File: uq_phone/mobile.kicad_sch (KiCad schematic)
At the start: 41 parts, among them J3 20279-001E-03, J4 20279-001E-03, J5 0786463001, Q1 MMBT3904, Q2 MMBT3904, U4 RC7620_1104625

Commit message: Update LCD, Add Programer, Shrink Footprints
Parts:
- R12, R17: value 4k7 -> 4.7k; footprint Resistor_SMD:R_0603_1608Metric -> Resistor_SMD:R_0402_1005Metric
- R13, R18: footprint Resistor_SMD:R_0603_1608Metric -> Resistor_SMD:R_0402_1005Metric
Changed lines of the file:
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@@
 		(pin "93"
 		)
-		(pin "244"
-		)
 		(pin "185"
 		)
@@
 		(pin "24"
 		)
-		(pin "243"
-		)
 		(pin "211"
 		)
@@
 		(pin "93"
 		)
-		(pin "244"
-		)
 		(pin "185"
 		)
@@
 		(pin "24"
 		)
-		(pin "243"
-		)
 		(pin "211"
 		)
@@
 			)
 		)
-		(property "Footprint" "Resistor_SMD:R_0603_1608Metric"
+		(property "Footprint" "Resistor_SMD:R_0402_1005Metric"
 			(at 67.31 257.81 0)
 			(effects
@@
 			)
 		)
-		(property "Description" ""
+		(property "Description" "RES SMD 47K OHM 1% 1/10W 0402"
 			(at 67.31 257.81 0)
 			(effects
@@
 	)
 	(symbol
-		(lib_name "RC7620_1104625_1")
 		(lib_id "RC7620_1104625:RC7620_1104625")
 		(at 200.66 97.79 0)
@@
 			)
 		)
-		(property "Value" "4k7"
+		(property "Value" "4.7k"
 			(at 115.57 246.38 90)
 			(effects
@@
 			)
 		)
-		(property "Footprint" "Resistor_SMD:R_0603_1608Metric"
+		(property "Footprint" "Resistor_SMD:R_0402_1005Metric"
 			(at 119.38 250.19 0)
 			(effects
@@
 			)
 		)
-		(property "Description" ""
+		(property "Description" "RES SMD 4.7K OHM 5% 1/10W 0402"
 			(at 119.38 250.19 0)
 			(effects
@@
 			)
 		)
-		(property "Footprint" "Resistor_SMD:R_0603_1608Metric"
+		(property "Footprint" "Resistor_SMD:R_0402_1005Metric"
 			(at 120.65 259.08 0)
 			(effects
@@
 			)
 		)
-		(property "Description" ""
+		(property "Description" "RES SMD 47K OHM 1% 1/10W 0402"
 			(at 120.65 259.08 0)
 			(effects
@@
 			)
 		)
-		(property "Value" "4k7"
+		(property "Value" "4.7k"
 			(at 62.23 245.11 90)
 			(effects
@@
 			)
 		)
-		(property "Footprint" "Resistor_SMD:R_0603_1608Metric"
+		(property "Footprint" "Resistor_SMD:R_0402_1005Metric"
 			(at 66.04 248.92 0)
 			(effects
@@
 			)
 		)
-		(property "Description" ""
+		(property "Description" "RES SMD 4.7K OHM 5% 1/10W 0402"
 			(at 66.04 248.92 0)
 			(effects

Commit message: Shrink More footprints, rearragment of PCB
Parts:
- C10, C11, C12, C13, C14, C15, C16, C8, C9: footprint Capacitor_SMD:C_0603_1608Metric -> Capacitor_SMD:C_0402_1005Metric
- R23, R24, R25: footprint Resistor_SMD:R_0603_1608Metric -> Resistor_SMD:R_0402_1005Metric
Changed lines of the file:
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@@
 			)
 		)
-		(property "Footprint" "Capacitor_SMD:C_0603_1608Metric"
+		(property "Footprint" "Capacitor_SMD:C_0402_1005Metric"
 			(at 311.15 220.98 0)
 			(effects
@@
 			)
 		)
-		(property "Description" ""
+		(property "Description" "CAP CER 22PF 16V X7R 0402"
 			(at 311.15 220.98 0)
 			(effects
@@
 			)
 		)
-		(property "Footprint" "Capacitor_SMD:C_0603_1608Metric"
+		(property "Footprint" "Capacitor_SMD:C_0402_1005Metric"
 			(at 325.12 220.98 0)
 			(effects
@@
 			)
 		)
-		(property "Description" ""
+		(property "Description" "0.1 µF ±10% 10V Ceramic Capacitor X7R 0402 (1005 Metric)"
 			(at 325.12 220.98 0)
 			(effects
@@
 			)
 		)
-		(property "Footprint" "Capacitor_SMD:C_0603_1608Metric"
+		(property "Footprint" "Capacitor_SMD:C_0402_1005Metric"
 			(at 304.8 220.98 0)
 			(effects
@@
 			)
 		)
-		(property "Description" ""
+		(property "Description" "CAP CER 22PF 16V X7R 0402"
 			(at 304.8 220.98 0)
 			(effects
@@
 			)
 		)
-		(property "Footprint" "Capacitor_SMD:C_0603_1608Metric"
+		(property "Footprint" "Capacitor_SMD:C_0402_1005Metric"
 			(at 330.2 220.98 0)
 			(effects
@@
 			)
 		)
-		(property "Description" ""
+		(property "Description" "CAP CER 33PF 16V X7R 0402"
 			(at 330.2 220.98 0)
 			(effects
@@
 			)
 		)
-		(property "Description" ""
+		(property "Description" "CAP CER 47UF 6.3V X5R 0805"
 			(at 361.95 41.91 0)
 			(effects
@@
 			)
 		)
-		(property "Footprint" "Capacitor_SMD:C_0603_1608Metric"
+		(property "Footprint" "Capacitor_SMD:C_0402_1005Metric"
 			(at 298.45 220.98 0)
 			(effects
@@
 			)
 		)
-		(property "Description" ""
+		(property "Description" "CAP CER 22PF 16V X7R 0402"
 			(at 298.45 220.98 0)
 			(effects
@@
 			)
 		)
-		(property "Footprint" "Capacitor_SMD:C_0603_1608Metric"
+		(property "Footprint" "Capacitor_SMD:C_0402_1005Metric"
 			(at 355.6 41.91 0)
 			(effects
@@
 			)
 		)
-		(property "Description" ""
+		(property "Description" "1 µF ±10% 25V Ceramic Capacitor X5R 0402 (1005 Metric)"
 			(at 355.6 41.91 0)
 			(effects
@@
 	)
 	(symbol
+		(lib_name "Resistor_22R_1")
 		(lib_id "Resistors:Resistor_22R")
 		(at 320.04 203.2 90)
@@
 			)
 		)
-		(property "Footprint" "Resistor_SMD:R_0603_1608Metric"
+		(property "Footprint" "Resistor_SMD:R_0402_1005Metric"
 			(at 323.85 203.2 0)
 			(effects
@@
 			)
 		)
-		(property "Description" ""
+		(property "Description" "RES SMD 22 OHM 1% 1/10W 0402"
 			(at 323.85 203.2 0)
 			(effects
@@
 	)
 	(symbol
+		(lib_name "Resistor_22R_2")
 		(lib_id "Resistors:Resistor_22R")
 		(at 320.04 205.74 90)
@@
 			)
 		)
-		(property "Footprint" "Resistor_SMD:R_0603_1608Metric"
+		(property "Footprint" "Resistor_SMD:R_0402_1005Metric"
 			(at 323.85 205.74 0)
 			(effects
@@
 			)
 		)
-		(property "Description" ""
+		(property "Description" "RES SMD 22 OHM 1% 1/10W 0402"
 			(at 323.85 205.74 0)
 			(effects
@@
 			)
 		)
-		(property "Footprint" "Capacitor_SMD:C_0603_1608Metric"
+		(property "Footprint" "Capacitor_SMD:C_0402_1005Metric"
 			(at 347.98 41.91 0)
 			(effects
@@
 			)
 		)
-		(property "Description" ""
+		(property "Description" "0.1 µF ±10% 10V Ceramic Capacitor X7R 0402 (1005 Metric)"
 			(at 347.98 41.91 0)
 			(effects
@@
 			)
 		)
-		(property "Description" ""
+		(property "Description" "CAP CER 47UF 6.3V X5R 0805"
 			(at 368.3 41.91 0)
 			(effects
@@
 			)
 		)
-		(property "Footprint" "Capacitor_SMD:C_0603_1608Metric"
+		(property "Footprint" "Capacitor_SMD:C_0402_1005Metric"
 			(at 335.28 41.91 0)
 			(effects
@@
 			)
 		)
-		(property "Description" ""
+		(property "Description" "CAP CER 10PF 16V X7R 0402"
 			(at 335.28 41.91 0)
 			(effects
@@
 			)
 		)
-		(property "Footprint" "Capacitor_SMD:C_0603_1608Metric"
+		(property "Footprint" "Capacitor_SMD:C_0402_1005Metric"
 			(at 341.63 41.91 0)
 			(effects
@@
 			)
 		)
-		(property "Description" ""
+		(property "Description" "10000 pF ±10% 16V Ceramic Capacitor X7R 0402 (1005 Metric)"
 			(at 341.63 41.91 0)
 			(effects
@@
 			)
 		)
-		(property "Footprint" "Resistor_SMD:R_0603_1608Metric"
+		(property "Footprint" "Resistor_SMD:R_0402_1005Metric"
 			(at 323.85 208.28 0)
 			(effects
@@
 			)
 		)
-		(property "Description" ""
+		(property "Description" "RES SMD 22 OHM 1% 1/10W 0402"
 			(at 323.85 208.28 0)
 			(effects

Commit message: Update PCB, minor changes
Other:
- note added: "Micro SIM card"
- note removed: "SIM card"
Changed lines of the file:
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@@
 		)
 	)
-	(text "SIM card"
+	(text "Micro SIM card"
 		(exclude_from_sim no)
 		(at 330.962 187.706 0)

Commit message: Changed SIM/uSD port & adjust routing
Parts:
- removed D2: ESDA6V1W5, ESDA6V1W5:SOT65P210X110-5N, symbol ESDA6V1W5:ESDA6V1W5
- removed J5: 0786463001, Sim_card:MOLEX_0786463001, symbol 0786463001:0786463001
- added J5: KP15B-6S-SF_800_, KP15B-6S-SF_800_:HIROSE_KP15B-6S-SF_800_, symbol KP15B-6S-SF_800_:KP15B-6S-SF_800_
- added R39: 10k, Resistor_SMD:R_0402_1005Metric, symbol Resistors:Resistor_10k
- added U13: TPD3F303DQDR, TPD3F303DQDR:SON40P170X135X80-9N, symbol TPD3F303DQDR:TPD3F303DQDR
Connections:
- net +1.8V: now also R39.2
- net GND: now also J5.C5_2 (GND), J5.G1 (GND__1), J5.G2 (GND__2), J5.S1 (SHIELD), J5.S10 (SHIELD__9), J5.S2 (SHIELD__1), J5.S3 (SHIELD__2), J5.S4 (SHIELD__3), J5.S5 (SHIELD__4), J5.S6 (SHIELD__5), J5.S7 (SHIELD__6), J5.S8 (SHIELD__7), J5.S9 (SHIELD__8), U13.9 (GND)
- net SIM_VDD: now also J5.C1_2 (VCC), U13.5 (VCC)
- net MOB_USB_N: now reaches R14.1, U4.12 (USB_D-)
- net MOB_USB_P: now reaches R15.1, U4.13 (USB_D+)
- net SIM_DET: now reaches U4.64 (UIM1_SIMA_DET)
- net SIM_DET: now also J5.D_T_2, R39.1
- net at R25.1: now also U13.7 (CLK_IN)
- net at R23.1: now also U13.6 (DATA2_IN)
- net at R24.1: now also U13.8 (DATA1_IN)
- new net: J5.C2_2 (RST), U13.1 (DATA1_OUT)
- new net: J5.C3_2 (CLK_2), U13.2 (CLK_OUT)
- new net: J5.C7_2 (I/O), U13.3 (DATA2_OUT)
- no-connect marks 39 -> 38

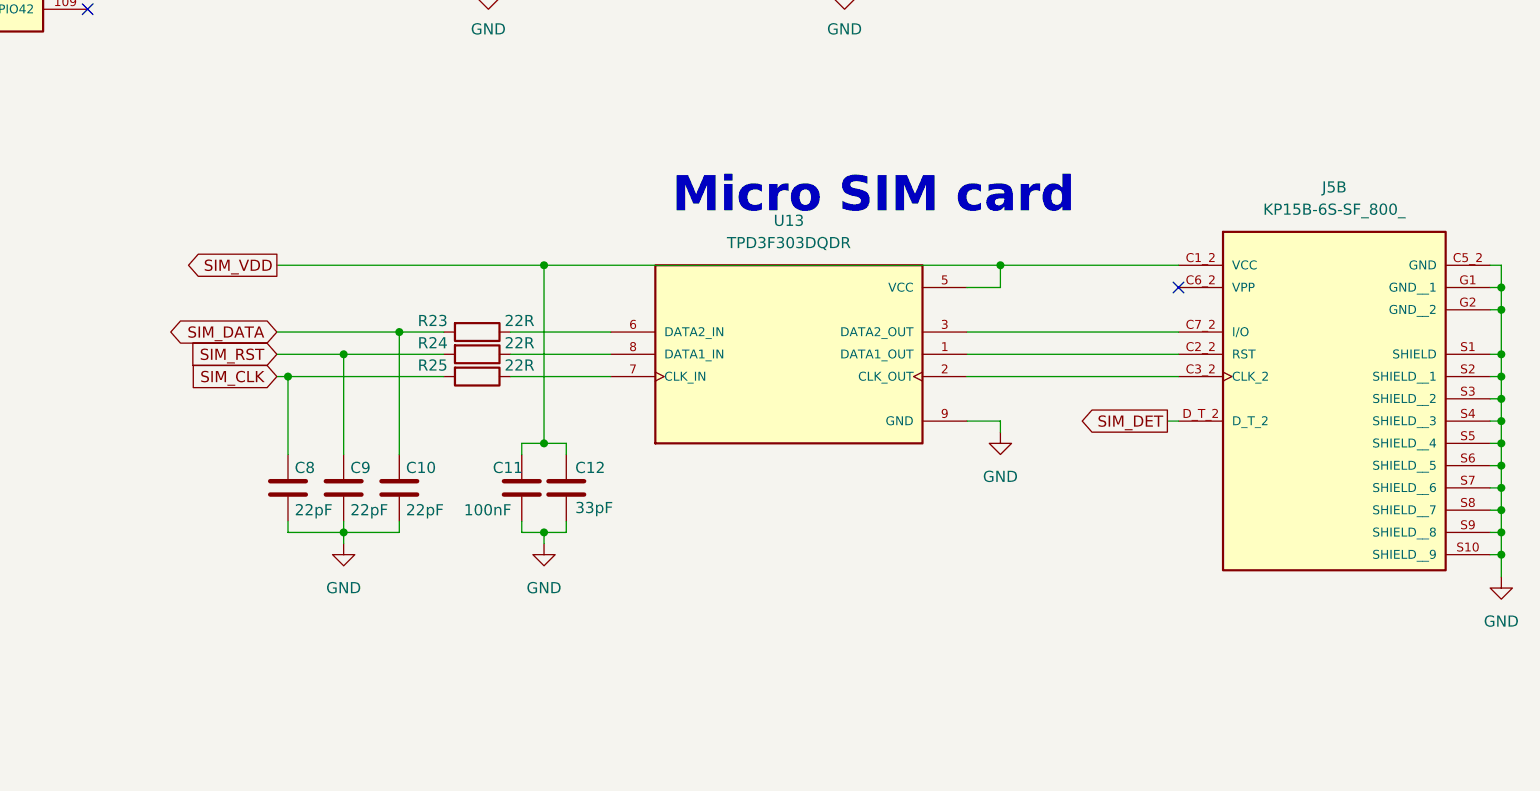
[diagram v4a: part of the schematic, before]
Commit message: Add LEDs, Inital Buttons
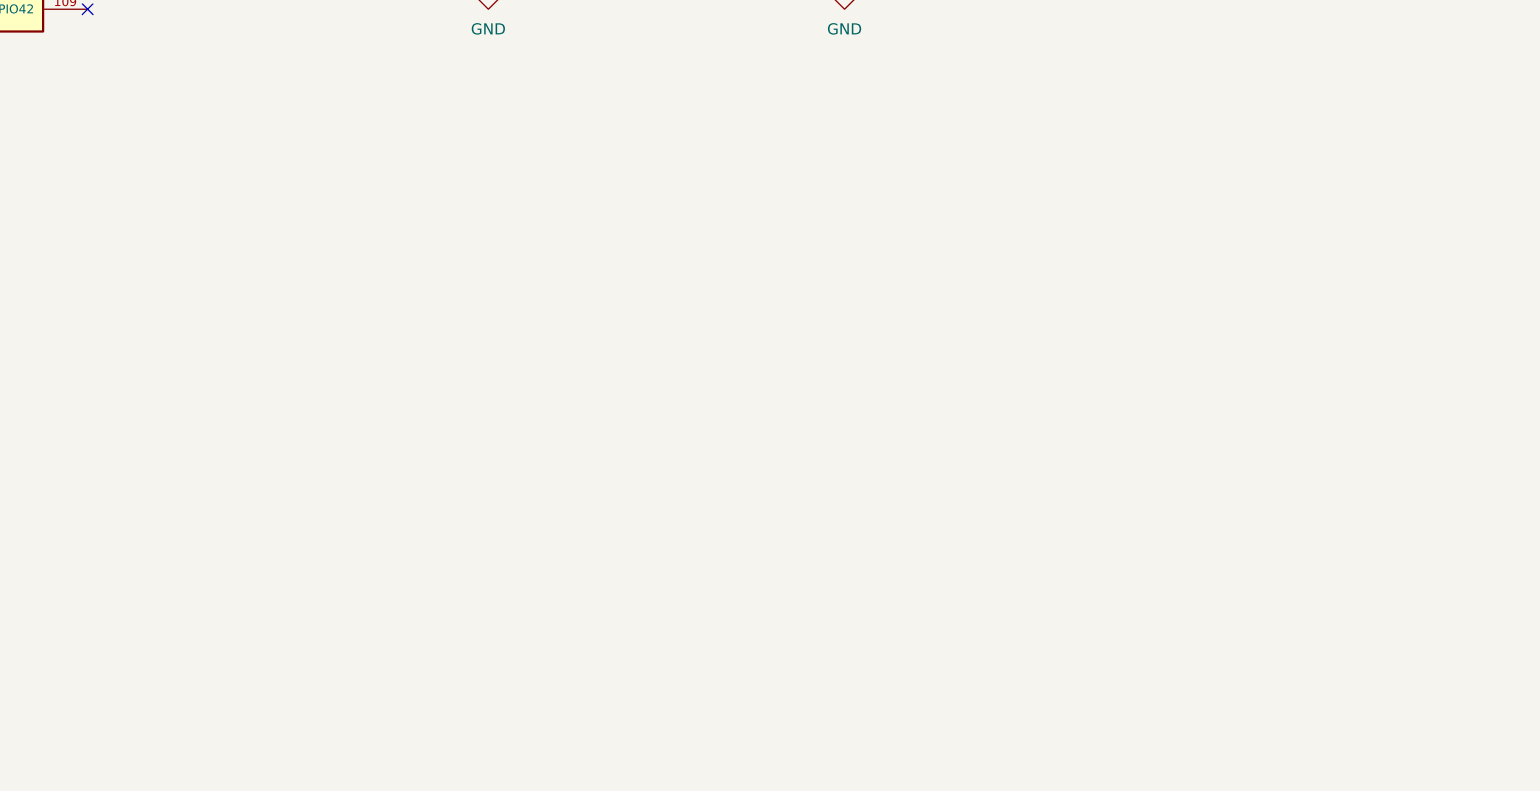
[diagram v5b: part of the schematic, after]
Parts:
- removed C10, C8, C9: 22pF, Capacitor_SMD:C_0402_1005Metric, symbol Capacitors:Capacitor_22pF
- removed C11: 100nF, Capacitor_SMD:C_0402_1005Metric, symbol Capacitors:capacitor_100nF
- removed C12: 33pF, Capacitor_SMD:C_0402_1005Metric, symbol Capacitors:Capacitor_33pF
- removed J5: KP15B-6S-SF_800_, KP15B-6S-SF_800_:HIROSE_KP15B-6S-SF_800_, symbol KP15B-6S-SF_800_:KP15B-6S-SF_800_
- removed R23, R24, R25: 22R, Resistor_SMD:R_0402_1005Metric, symbol Resistors:Resistor_22R
- removed U13: TPD3F303DQDR, TPD3F303DQDR:SON40P170X135X80-9N, symbol TPD3F303DQDR:TPD3F303DQDR
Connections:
- no-connect marks 38 -> 37
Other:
- note removed: "Micro SIM card"

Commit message: Routing Init
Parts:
- removed Q1, Q2: MMBT3904, MMBT3904LT1G:SOT95P240X111-3N, symbol MMBT3904LT1G:MMBT3904LT1G
- added Q1, Q2: MMBT3904LP-7, MMBT3904LP-7:DFN101X61X53-3N, symbol MMBT3904LP-7:MMBT3904LP-7
- renumbered C15 to C10, C16 to C11, C17 to C12, C18 to C13, C13 to C8, C14 to C9, R39 to R23
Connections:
- net GND: now also U4.P1, U4.P10, U4.P11, U4.P12, U4.P13, U4.P14, U4.P15, U4.P16, U4.P17, U4.P18, U4.P19, U4.P2, U4.P20, U4.P3, U4.P4, U4.P5, U4.P6, U4.P7, U4.P8, U4.P9, Q1.2, Q2.2
- net MOB_PWR: now also Q1.3
- net MOB_RST: now also Q2.3
- net at R12.1, R13.2: now also Q1.1
- net at R17.1, R18.2: now also Q2.1
- net MOB_GNSS_ANT: no longer names the net of U4.38 (RF_GNSS)
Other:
- moved on the sheet: C10, C11, C12, C13, C8, C9, J3, J4, R14, R15, R16, R19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

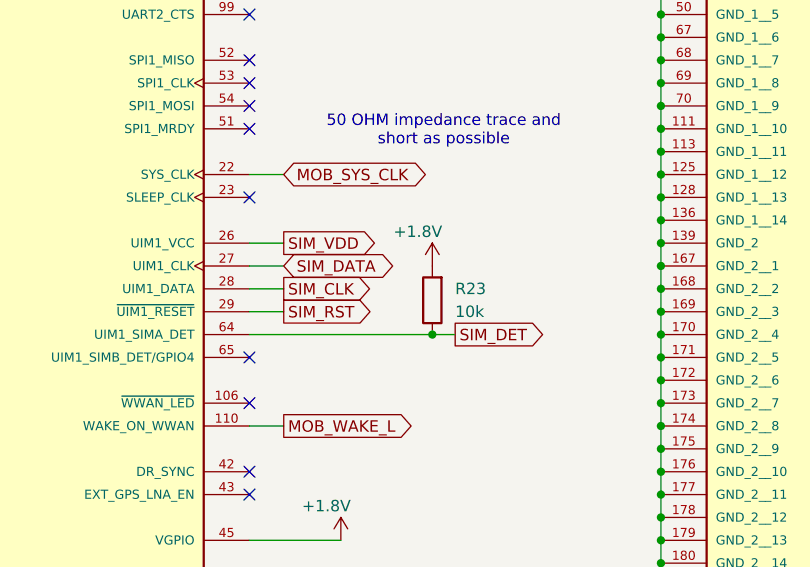
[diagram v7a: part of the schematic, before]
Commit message: Update pcb and remove Stm32 profile
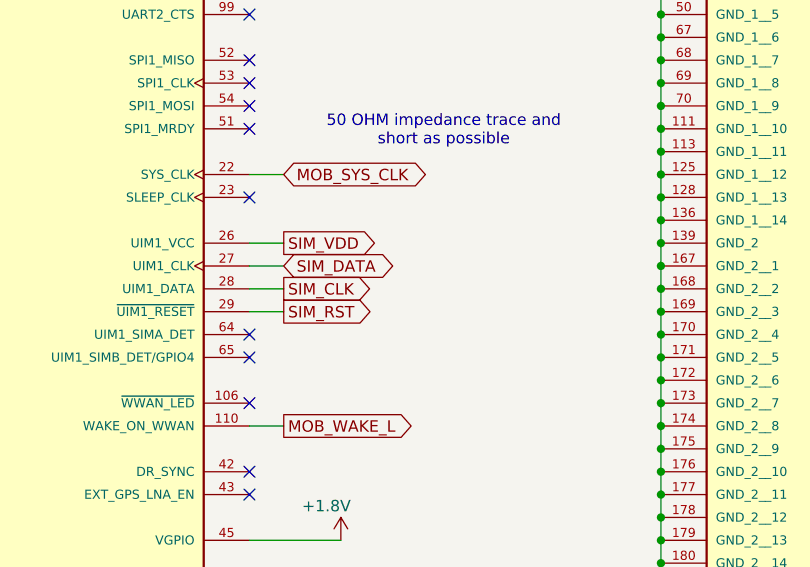
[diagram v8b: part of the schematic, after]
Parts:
- removed R23: 10k, Resistor_SMD:R_0402_1005Metric, symbol Resistors:Resistor_10k
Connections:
- net SIM_DET: no longer names the net of U4.64 (UIM1_SIMA_DET)
- no-connect marks 37 -> 38
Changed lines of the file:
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@@
 	)
 	(junction
-		(at 184.15 93.98)
-		(diameter 0)
-		(color 0 0 0 0)
-	)
-	(junction
 		(at 250.19 111.76)
 		(diameter 0)
@@
 	)
 	(no_connect
+		(at 163.83 93.98)
+	)
+	(no_connect
 		(at 82.55 152.4)
 	)
@@
 	(wire
 		(pts
-			(xy 163.83 93.98) (xy 184.15 93.98)
-		)
-		(stroke
-			(width 0)
-			(type default)
-		)
-	)
-	(wire
-		(pts
 			(xy 77.47 104.14) (xy 82.55 104.14)
 		)
@@
 	(wire
 		(pts
-			(xy 184.15 93.98) (xy 186.69 93.98)
-		)
-		(stroke
-			(width 0)
-			(type default)
-		)
-	)
-	(wire
-		(pts
 			(xy 82.55 88.9) (xy 29.21 88.9)
 		)
@@
 		)
 	)
-	(global_label "SIM_DET"
-		(shape output)
-		(at 186.69 93.98 0)
-		(fields_autoplaced yes)
-		(effects
-			(font
-				(size 1.27 1.27)
-			)
-			(justify left)
-		)
-		(property "Intersheetrefs" "${INTERSHEET_REFS}"
-			(at 197.2951 93.98 0)
-			(effects
-				(font
-					(size 1.27 1.27)
-				)
-				(justify left)
-				(hide yes)
-			)
-		)
-	)
 	(global_label "MOB_AUD_IN"
 		(shape input)
@@
 					(unit 1)
 				)
-			)
-		)
-	)
-	(symbol
-		(lib_id "power:+1V8")
-		(at 184.15 86.36 0)
-		(unit 1)
-		(exclude_from_sim no)
-		(in_bom yes)
-		(on_board yes)
-		(dnp no)
-		(property "Reference" "#PWR042"
-			(at 184.15 90.17 0)
-			(effects
-				(font
-					(size 1.27 1.27)
-				)
-				(hide yes)
-			)
-		)
-		(property "Value" "+1.8V"
-			(at 179.832 82.55 0)
-			(effects
-				(font
-					(size 1.27 1.27)
-				)
-				(justify left)
-			)
-		)
-		(property "Footprint" ""
-			(at 184.15 86.36 0)
-			(effects
-				(font
-					(size 1.27 1.27)
-				)
-				(hide yes)
-			)
-		)
-		(property "Datasheet" ""
-			(at 184.15 86.36 0)
-			(effects
-				(font
-					(size 1.27 1.27)
-				)
-				(hide yes)
-			)
-		)
-		(property "Description" "Power symbol creates a global label with name \"+1V8\""
-			(at 184.15 86.36 0)
-			(effects
-				(font
-					(size 1.27 1.27)
-				)
-				(hide yes)
-			)
-		)
-		(pin "1"
-		)
-		(instances
-			(project "uq_phone"
-				(path "/14f57415-6807-40a5-bb38-3cb818a2cdae/7b044aa4-5304-4653-927f-15b0f7e69857"
-					(reference "#PWR042")
-					(unit 1)
-				)
-			)
-		)
-	)
-	(symbol
-		(lib_id "Resistors:Resistor_10k")
-		(at 184.15 90.17 0)
-		(unit 1)
-		(exclude_from_sim no)
-		(in_bom yes)
-		(on_board yes)
-		(dnp no)
-		(fields_autoplaced yes)
-		(property "Reference" "R23"
-			(at 186.69 88.8999 0)
-			(effects
-				(font
-					(size 1.27 1.27)
-				)
-				(justify left)
-			)
-		)
-		(property "Value" "10k"
-			(at 186.69 91.4399 0)
-			(effects
-				(font
-					(size 1.27 1.27)
-				)
-				(justify left)
-			)
-		)
-		(property "Footprint" "Resistor_SMD:R_0402_1005Metric"
-			(at 184.15 93.98 0)
-			(effects
-				(font
-					(size 1.27 1.27)
-				)
-				(hide yes)
-			)
-		)
-		(property "Datasheet" ""
-			(at 184.15 93.98 0)
-			(effects
-				(font
-					(size 1.27 1.27)
-				)
-				(hide yes)
-			)
-		)
-		(property "Description" "RES SMD 10K OHM 1% 1/10W 0402"
-			(at 184.15 93.98 0)
-			(effects
-				(font
-					(size 1.27 1.27)
-				)
-				(hide yes)
-			)
-		)
-		(pin "2"
-		)
-		(pin "1"
-		)
-		(instances
-			(project ""
-				(path "/14f57415-6807-40a5-bb38-3cb818a2cdae/7b044aa4-5304-4653-927f-15b0f7e69857"
-					(reference "R23")
-					(unit 1)
-				)
